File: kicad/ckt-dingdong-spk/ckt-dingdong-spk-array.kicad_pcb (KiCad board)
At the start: 2 copper layers, 40.6 x 180.3 mm, 170 parts, among them J1 SM04B-SRSS

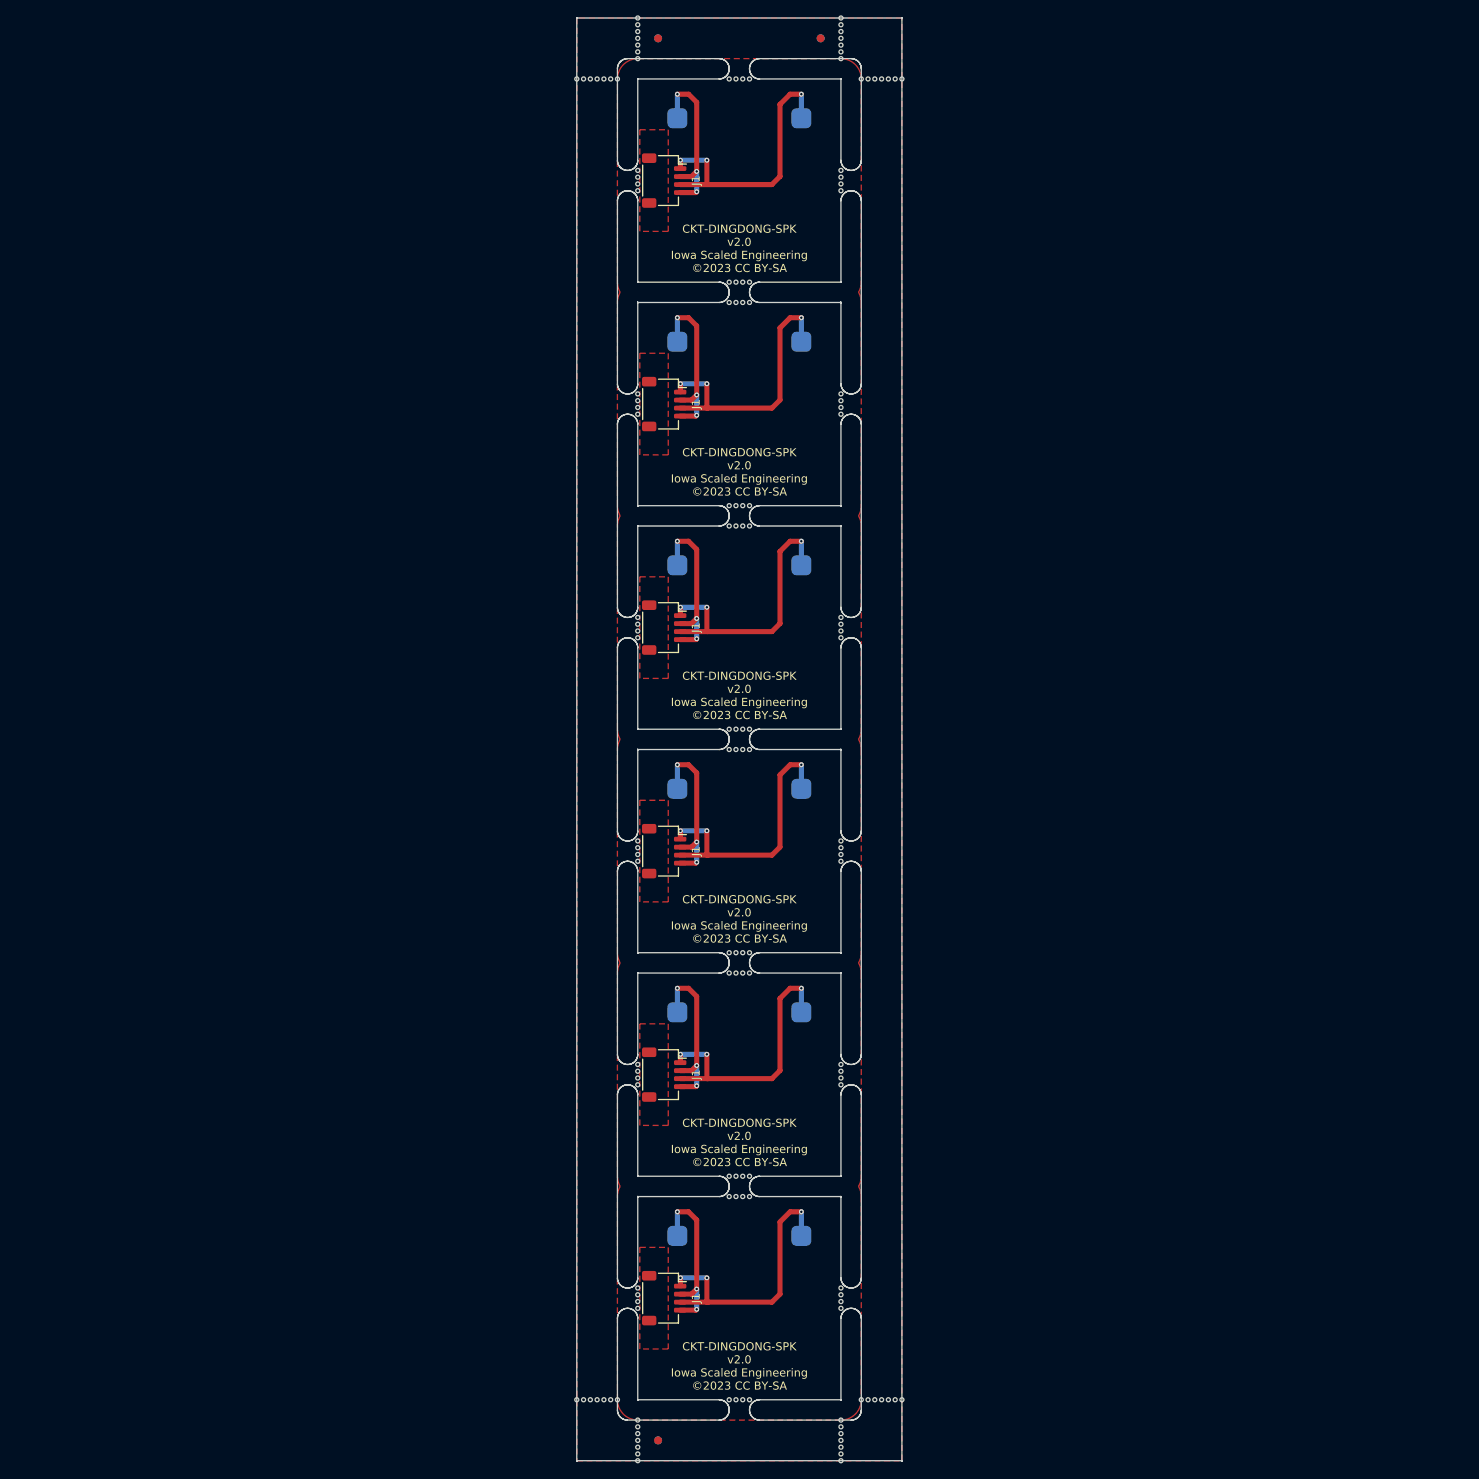
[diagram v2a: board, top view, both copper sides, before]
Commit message: Changed to horizontal array and removed half the tabs
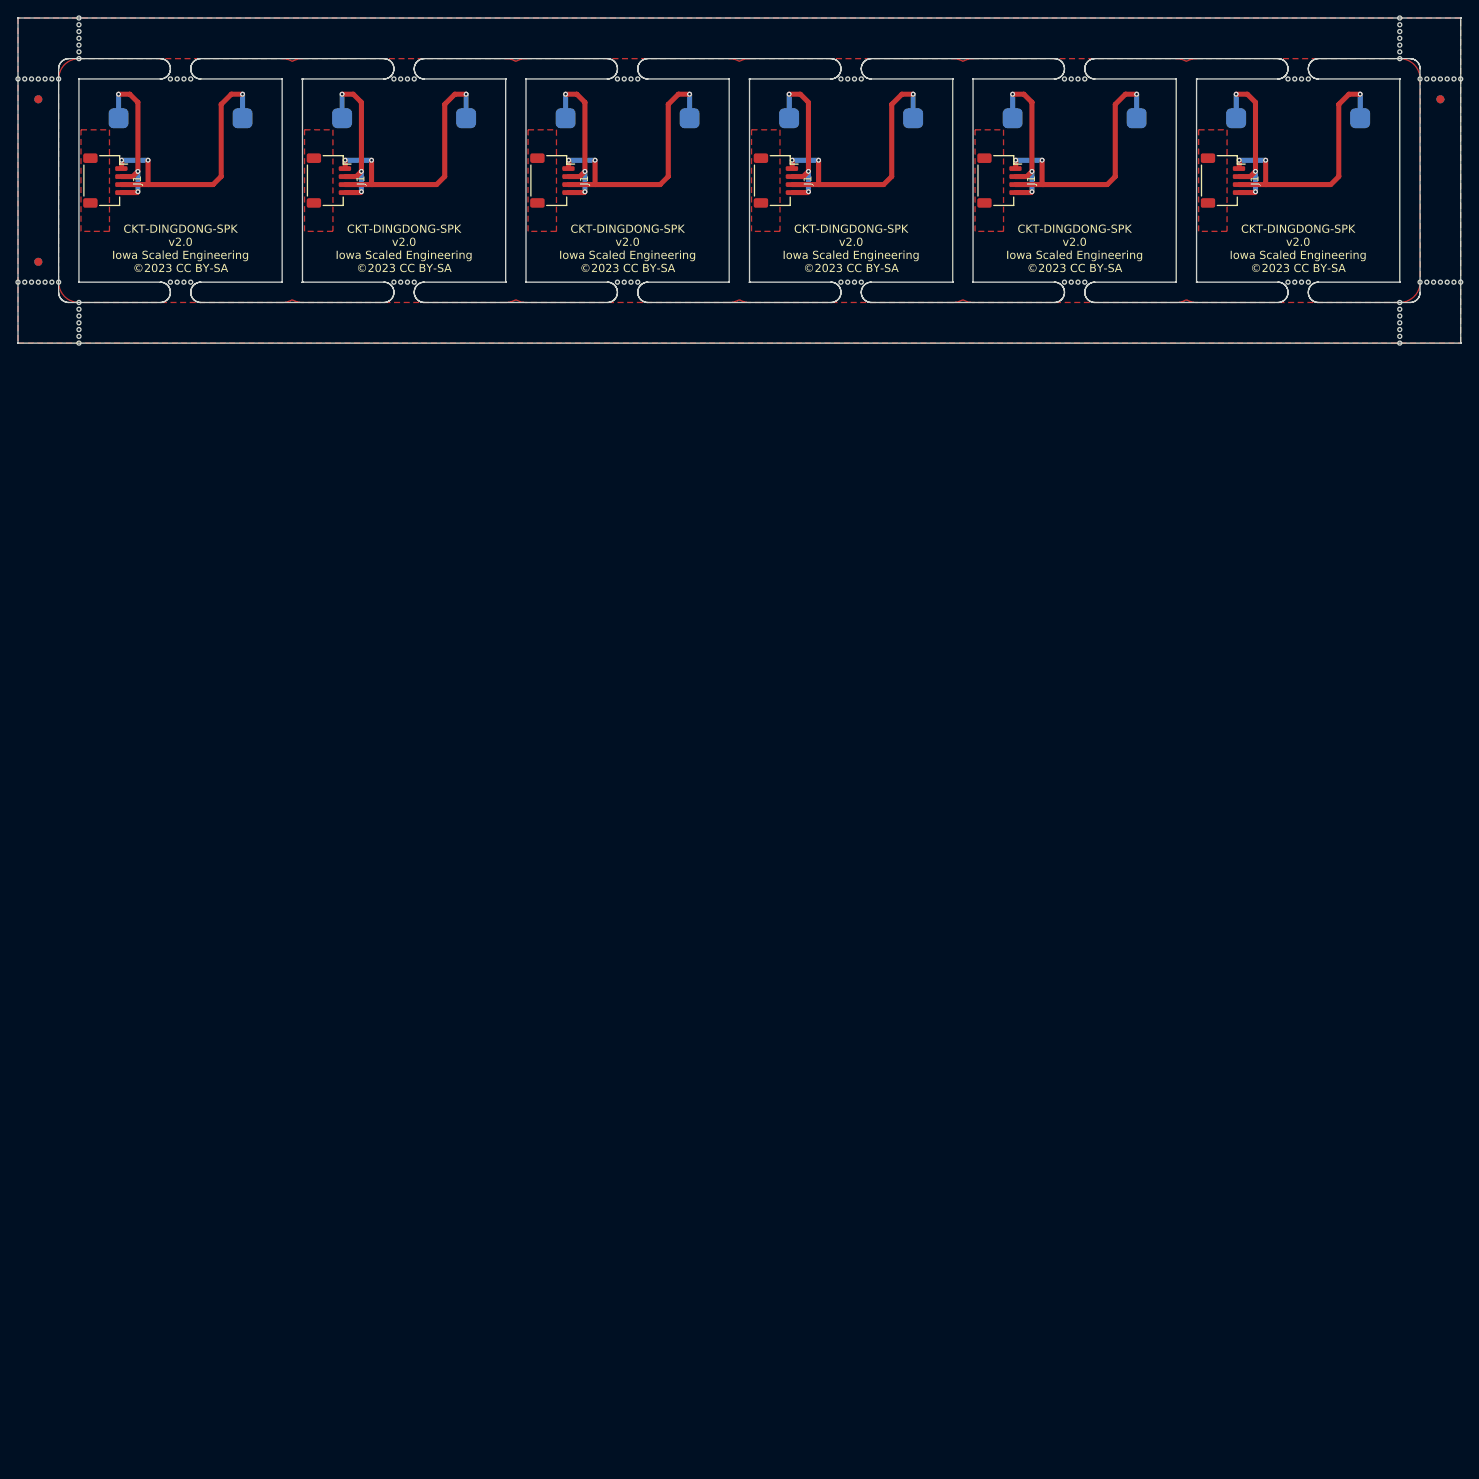
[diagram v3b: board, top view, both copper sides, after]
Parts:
- removed the REF** at (129.0, 192.7)
- removed the REF** at (130.7, 27.6)
- removed the REF** at (133.3, 192.7)
- removed the REF** at (166.3, 192.7)
- removed the REF** at (135.8, 200.3)
- removed the REF** at (163.7, 192.7)
- removed the REF** at (161.2, 21.7)
- removed the REF** at (165.4, 192.7)
- removed the REF** at (135.8, 198.6)
- removed the REF** at (168.0, 192.7)
- removed the REF** at (129.9, 27.6)
- removed the REF** at (133.3, 27.6)
- removed the REF** at (128.2, 27.6)
- removed the REF** at (167.1, 27.6)
- removed the REF** at (167.1, 192.7)
- removed the REF** at (168.8, 192.7)
- removed the REF** at (131.6, 27.6)
- removed the REF** at (131.6, 192.7)
- removed the REF** at (168.8, 27.6)
- removed the REF** at (161.2, 25.1)
- removed the REF** at (164.6, 192.7)
- removed the REF** at (163.7, 27.6)
- removed the REF** at (165.4, 27.6)
- removed the REF** at (161.2, 20.8)
- removed the REF** at (168.0, 27.6)
- removed the REF** at (161.2, 196.1)
- removed the REF** at (166.3, 27.6)
- removed the REF** at (161.2, 199.5)
- removed the REF** at (129.9, 192.7)
- removed the REF** at (161.2, 22.5)
- removed the REF** at (161.2, 24.2)
- removed the REF** at (129.0, 27.6)
- removed the REF** at (132.4, 27.6)
- removed the REF** at (135.8, 195.3)
- removed the REF** at (161.2, 197.0)
- removed the REF** at (161.2, 195.3)
- removed the REF** at (128.2, 192.7)
- removed the REF** at (135.8, 199.5)
- removed the REF** at (161.2, 200.3)
- removed the REF** at (135.8, 197.0)
- removed the REF** at (135.8, 197.8)
- removed the REF** at (164.6, 27.6)
- removed the REF** at (135.8, 196.1)
- removed the REF** at (161.2, 197.8)
- removed the REF** at (130.7, 192.7)
- removed the REF** at (161.2, 23.4)
- removed the REF** at (132.4, 192.7)
- removed the REF** at (161.2, 198.6)
- moved REF** 188.3 mm to (237.8, 27.6)
- moved REF** 187.5 mm to (237.0, 27.6)
- moved REF** 186.7 mm to (236.1, 27.6)
- moved REF** 185.9 mm to (235.3, 27.6)
- moved REF** 170.6 mm to (61.7, 27.6)
- moved REF** 169.5 mm to (62.6, 27.6)
- moved REF** 168.3 mm to (63.4, 27.6)
- moved REF** 166.4 mm to (60.9, 50.5) (x2)
- moved REF** 164.8 mm to (58.3, 27.6)
- moved REF** 163.9 mm to (59.2, 27.6)
- moved REF** 163.4 mm to (233.6, 27.6)
- moved REF** 163.4 mm to (234.4, 27.6)
- moved REF** 163.0 mm to (60.0, 27.6)
- moved REF** 162.3 mm to (61.7, 53.0)
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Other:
- board size 40.6 x 180.3 mm -> 180.3 x 40.6 mm

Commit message: Changed to 10x array
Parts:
- removed the REF** at (66.0, 56.4)
- removed the REF** at (66.0, 57.3)
- removed the REF** at (66.0, 22.5)
- removed the REF** at (63.4, 27.6)
- removed the REF** at (63.4, 53.0)
- removed the REF** at (60.9, 30.2) (x2)
- removed the REF** at (60.9, 50.5)
- removed the REF** at (236.1, 30.2) (x2)
- removed the REF** at (66.0, 59.8)
- removed the REF** at (59.2, 27.6)
- removed the REF** at (231.1, 58.1)
- removed the REF** at (238.7, 27.6)
- removed the REF** at (237.8, 27.6)
- removed the REF** at (236.1, 27.6)
- removed the REF** at (231.1, 24.2)
- removed the REF** at (231.1, 20.0)
- removed the REF** at (61.7, 27.6)
- removed the REF** at (62.6, 53.0)
- removed the REF** at (231.1, 25.1)
- removed the REF** at (66.0, 55.6)
- removed the REF** at (78.2, 27.6)
- removed the REF** at (235.3, 53.0)
- removed the REF** at (58.3, 27.6)
- removed the REF** at (66.0, 23.4)
- removed the REF** at (234.4, 53.0)
- removed the REF** at (59.2, 53.0)
- removed the REF** at (236.1, 53.0)
- removed the REF** at (231.1, 60.6)
- removed the REF** at (60.9, 27.6)
- removed the REF** at (231.1, 22.5)
- removed the REF** at (231.1, 57.3)
- removed the REF** at (233.6, 27.6)
- removed the REF** at (66.0, 58.1)
- removed the REF** at (231.1, 56.4)
- removed the REF** at (237.8, 53.0)
- removed the REF** at (66.0, 24.2)
- removed the REF** at (66.0, 21.7)
- removed the REF** at (231.1, 20.8)
- removed the REF** at (231.1, 23.4)
- removed the REF** at (231.1, 59.8)
- removed the REF** at (231.1, 21.7)
- removed the REF** at (237.0, 27.6)
- removed the REF** at (62.6, 27.6)
- removed the REF** at (231.1, 55.6)
- removed the REF** at (60.0, 27.6)
- removed the REF** at (60.0, 53.0)
- removed the REF** at (60.9, 53.0)
- removed the REF** at (61.7, 53.0)
- removed the REF** at (234.4, 27.6)
- removed the REF** at (233.6, 53.0)
- removed the REF** at (78.2, 53.0)
- removed the REF** at (237.0, 53.0)
- removed the REF** at (58.3, 53.0)
- removed the REF** at (66.0, 20.0)
- removed the REF** at (66.0, 58.9)
- removed the REF** at (238.7, 53.0)
- removed the REF** at (66.0, 60.6)
- removed the REF** at (235.3, 27.6)
- removed the REF** at (66.0, 20.8)
- removed the REF** at (231.1, 58.9)
- removed the REF** at (66.0, 25.1)
- added J1: SM04B-SRSS, Connector_JST:JST_SH_SM04B-SRSS-TB_1x04-1MP_P1.00mm_Horizontal, F.Cu at (209.0, 40.3)
- added J1: SM04B-SRSS, Connector_JST:JST_SH_SM04B-SRSS-TB_1x04-1MP_P1.00mm_Horizontal, F.Cu at (264.8, 40.3)
- added J1: SM04B-SRSS, Connector_JST:JST_SH_SM04B-SRSS-TB_1x04-1MP_P1.00mm_Horizontal, F.Cu at (236.9, 40.3)
- added J1: SM04B-SRSS, Connector_JST:JST_SH_SM04B-SRSS-TB_1x04-1MP_P1.00mm_Horizontal, F.Cu at (181.0, 40.3)
- added REF**: NPTH, NPTH, F.Cu at (10.1, 58.9)
- added REF**: NPTH, NPTH, F.Cu at (4.99, 27.6)
- added REF**: NPTH, NPTH, F.Cu at (247.6, 53.0)
- added REF**: NPTH, NPTH, F.Cu at (273.8, 27.6)
- added REF**: NPTH, NPTH, F.Cu at (286.9, 24.2)
- added REF**: NPTH, NPTH, F.Cu at (273.8, 53.0)
- added REF**: NPTH, NPTH, F.Cu at (6.68, 27.6)
- added REF**: NPTH, NPTH, F.Cu at (245.9, 53.0)
- added REF**: NPTH, NPTH, F.Cu at (78.2, 27.6)
- added REF**: NPTH, NPTH, F.Cu at (286.9, 25.1)
- added REF**: NPTH, NPTH, F.Cu at (10.1, 60.6)
- added REF**: NPTH, NPTH, F.Cu at (10.1, 59.8)
- added REF**: NPTH, NPTH, F.Cu at (286.9, 20.8)
- added REF**: Fiducial, Fiducial, F.Cu at (4.99, 50.5)
- added REF**: NPTH, NPTH, F.Cu at (245.9, 27.6)
- added REF**: NPTH, NPTH, F.Cu at (5.84, 27.6)
- added REF**: NPTH, NPTH, F.Cu at (3.30, 53.0)
- added REF**: NPTH, NPTH, F.Cu at (292.0, 27.6)
- added REF**: NPTH, NPTH, F.Cu at (293.7, 53.0)
- added REF**: NPTH, NPTH, F.Cu at (10.1, 23.4)
- added REF**: NPTH, NPTH, F.Cu at (10.1, 56.4)
- added REF**: NPTH, NPTH, F.Cu at (286.9, 21.7)
- added REF**: NPTH, NPTH, F.Cu at (7.53, 27.6)
- added REF**: NPTH, NPTH, F.Cu at (294.6, 27.6)
- added REF**: NPTH, NPTH, F.Cu at (275.5, 53.0)
- added REF**: Fiducial, Fiducial, F.Cu at (4.99, 30.2)
- added REF**: NPTH, NPTH, F.Cu at (286.9, 60.6)
- added REF**: NPTH, NPTH, F.Cu at (286.9, 56.4)
- added REF**: NPTH, NPTH, F.Cu at (24.0, 53.0)
- added REF**: NPTH, NPTH, F.Cu at (4.14, 53.0)
- added REF**: NPTH, NPTH, F.Cu at (49.4, 53.0)
- added REF**: Fiducial, Fiducial, B.Cu at (4.99, 50.5)
- added REF**: Fiducial, Fiducial, B.Cu at (292.0, 30.2)
- added REF**: Fiducial, Fiducial, B.Cu at (4.99, 30.2)
- added REF**: NPTH, NPTH, F.Cu at (289.5, 27.6)
- added REF**: NPTH, NPTH, F.Cu at (274.7, 53.0)
- added REF**: NPTH, NPTH, F.Cu at (275.5, 27.6)
- added REF**: NPTH, NPTH, F.Cu at (6.68, 53.0)
- added REF**: NPTH, NPTH, F.Cu at (273.0, 27.6)
- added REF**: NPTH, NPTH, F.Cu at (286.9, 22.5)
- added REF**: NPTH, NPTH, F.Cu at (286.9, 20.0)
- added REF**: NPTH, NPTH, F.Cu at (286.9, 58.9)
- added REF**: NPTH, NPTH, F.Cu at (10.1, 20.8)
- added REF**: NPTH, NPTH, F.Cu at (291.2, 27.6)
- added REF**: NPTH, NPTH, F.Cu at (21.5, 27.6)
- added REF**: NPTH, NPTH, F.Cu at (10.1, 55.6)
- added REF**: NPTH, NPTH, F.Cu at (292.9, 53.0)
- added REF**: NPTH, NPTH, F.Cu at (51.1, 53.0)
- added REF**: NPTH, NPTH, F.Cu at (286.9, 55.6)
- added REF**: NPTH, NPTH, F.Cu at (274.7, 27.6)
- added REF**: NPTH, NPTH, F.Cu at (10.1, 24.2)
- added REF**: NPTH, NPTH, F.Cu at (286.9, 58.1)
- added REF**: NPTH, NPTH, F.Cu at (10.1, 20.0)
- added REF**: NPTH, NPTH, F.Cu at (273.0, 53.0)
- added REF**: NPTH, NPTH, F.Cu at (293.7, 27.6)
- added REF**: NPTH, NPTH, F.Cu at (78.2, 53.0)
- added REF**: NPTH, NPTH, F.Cu at (2.45, 27.6)
- added REF**: NPTH, NPTH, F.Cu at (4.14, 27.6)
- added REF**: NPTH, NPTH, F.Cu at (49.4, 27.6)
- added REF**: NPTH, NPTH, F.Cu at (23.2, 53.0)
- added REF**: NPTH, NPTH, F.Cu at (246.7, 27.6)
- added REF**: NPTH, NPTH, F.Cu at (50.3, 27.6)
- added REF**: NPTH, NPTH, F.Cu at (294.6, 53.0)
- added REF**: NPTH, NPTH, F.Cu at (10.1, 21.7)
- added REF**: NPTH, NPTH, F.Cu at (24.0, 27.6)
- added REF**: NPTH, NPTH, F.Cu at (246.7, 53.0)
- added REF**: NPTH, NPTH, F.Cu at (286.9, 23.4)
- added REF**: NPTH, NPTH, F.Cu at (22.3, 53.0)
- added REF**: NPTH, NPTH, F.Cu at (52.0, 53.0)
- added REF**: NPTH, NPTH, F.Cu at (290.3, 53.0)
- added REF**: NPTH, NPTH, F.Cu at (52.0, 27.6)
- added REF**: NPTH, NPTH, F.Cu at (290.3, 27.6)
- added REF**: NPTH, NPTH, F.Cu at (10.1, 57.3)
- added REF**: NPTH, NPTH, F.Cu at (292.0, 53.0)
- added REF**: NPTH, NPTH, F.Cu at (289.5, 53.0)
- added REF**: NPTH, NPTH, F.Cu at (10.1, 22.5)
- added REF**: NPTH, NPTH, F.Cu at (7.53, 53.0)
- added REF**: NPTH, NPTH, F.Cu at (21.5, 53.0)
- added REF**: NPTH, NPTH, F.Cu at (291.2, 53.0)
- added REF**: NPTH, NPTH, F.Cu at (2.45, 53.0)
- added REF**: NPTH, NPTH, F.Cu at (5.84, 53.0)
- added REF**: NPTH, NPTH, F.Cu at (245.0, 53.0)
- added REF**: NPTH, NPTH, F.Cu at (247.6, 27.6)
- added REF**: NPTH, NPTH, F.Cu at (51.1, 27.6)
- added REF**: NPTH, NPTH, F.Cu at (10.1, 25.1)
- added REF**: Fiducial, Fiducial, F.Cu at (292.0, 30.2)
- added REF**: NPTH, NPTH, F.Cu at (22.3, 27.6)
- added REF**: NPTH, NPTH, F.Cu at (10.1, 58.1)
- added REF**: NPTH, NPTH, F.Cu at (50.3, 53.0)
- added REF**: NPTH, NPTH, F.Cu at (4.99, 53.0)
- added REF**: NPTH, NPTH, F.Cu at (23.2, 27.6)
- added REF**: NPTH, NPTH, F.Cu at (286.9, 57.3)
- added REF**: NPTH, NPTH, F.Cu at (245.0, 27.6)
- added REF**: NPTH, NPTH, F.Cu at (3.30, 27.6)
- added REF**: NPTH, NPTH, F.Cu at (286.9, 59.8)
- added REF**: NPTH, NPTH, F.Cu at (292.9, 27.6)
- added SPK1: Speaker, ISE_Generic:Speaker_13x18, B.Cu at (246.3, 37.8)
- added SPK1: Speaker, ISE_Generic:Speaker_13x18, B.Cu at (274.2, 37.8)
- added SPK1: Speaker, ISE_Generic:Speaker_13x18, B.Cu at (218.3, 37.8)
- SPK1: renamed from REF**; value Fiducial -> Speaker; footprint Fiducial -> ISE_Generic:Speaker_13x18; moved to B.Cu
- moved SPK1 130.2 mm to (190.4, 37.8), turned to 180 degrees
- moved J1 55.9 mm to (97.2, 40.3)
- moved J1 55.9 mm to (69.3, 40.3)
- moved SPK1 55.9 mm to (22.8, 37.8)
- moved SPK1 55.9 mm to (50.7, 37.8)
- moved J1 55.9 mm to (41.3, 40.3)
- moved J1 55.9 mm to (13.4, 40.3)
- moved J1 55.9 mm to (125.1, 40.3)
- moved J1 55.9 mm to (153.1, 40.3)
- moved SPK1 55.9 mm to (134.5, 37.8)
- moved SPK1 55.9 mm to (106.6, 37.8)
- moved SPK1 55.9 mm to (78.7, 37.8)
- moved SPK1 55.9 mm to (162.5, 37.8)
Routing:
- net Board_9-Net-(SPK1-Pad1): track 0.00 -> 35.5 mm, vias 0 -> 3
- net Board_8-Net-(SPK1-Pad1): track 0.00 -> 35.5 mm, vias 0 -> 3
- net Board_7-Net-(SPK1-Pad1): track 0.00 -> 35.5 mm, vias 0 -> 3
- net Board_6-Net-(SPK1-Pad1): track 0.00 -> 35.5 mm, vias 0 -> 3
- net Board_9-Net-(SPK1-Pad2): track 0.00 -> 21.5 mm, vias 0 -> 3
- net Board_8-Net-(SPK1-Pad2): track 0.00 -> 21.5 mm, vias 0 -> 3
- net Board_7-Net-(SPK1-Pad2): track 0.00 -> 21.5 mm, vias 0 -> 3
- net Board_6-Net-(SPK1-Pad2): track 0.00 -> 21.5 mm, vias 0 -> 3
- added copper zone on F.Cu, net Board_6-/MP
- added copper zone on F.Cu, net Board_7-/MP
- added copper zone on F.Cu, net Board_8-/MP
- added copper zone on F.Cu, net Board_9-/MP
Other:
- board size 180.3 x 40.6 mm -> 292.1 x 40.6 mm
